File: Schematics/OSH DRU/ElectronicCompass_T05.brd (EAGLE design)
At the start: 50.5 x 50.8 mm, 69 parts, among them Q1 FDN360P, Q2 FDN360P, Q3 FDN360P, Q4 FDN360P, Q5 BC817-16LT1SMD, Q6 BC817-16LT1SMD, U1 ATMEGA32U4, U2 LTC4067, X1 USBSMD, Y1 16MHz

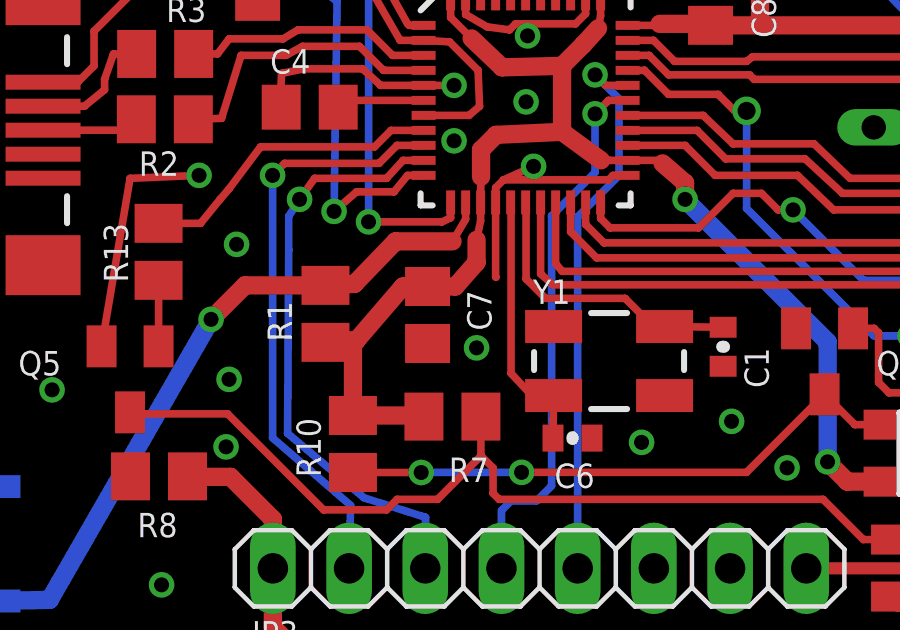
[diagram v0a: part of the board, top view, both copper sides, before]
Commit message: Removed capacitor
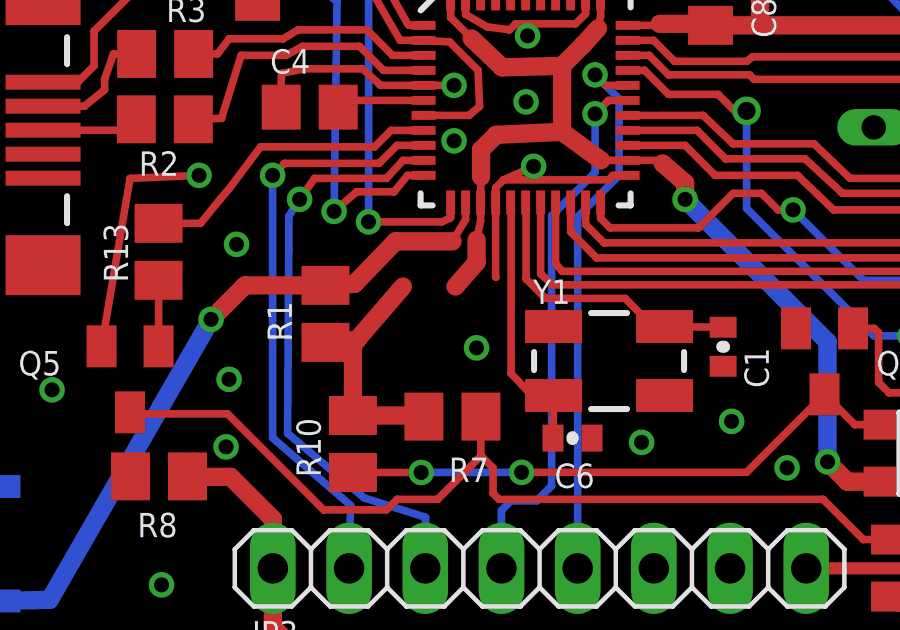
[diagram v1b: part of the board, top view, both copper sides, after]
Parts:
- removed C7: 0.1uF, rcl:C0805
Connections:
- net GND: no longer C7.2
- net VCC: no longer C7.1
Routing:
- net VCC: track 92.1 -> 90.3 mm
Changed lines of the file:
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@@
 <attribute name="NAME" x="27.2365" y="9.84275" size="0.8128" layer="25" rot="R180"/>
-</element>
-<element name="C7" library="rcl" package="C0805" value="0.1uF" x="21.66625" y="14.795" smashed="yes" rot="R270">
-<attribute name="NAME" x="22.98625" y="15.615" size="0.8128" layer="25" rot="R270"/>
 </element>
 <element name="R7" library="resistor" package="M0805" value="1M" x="22.495" y="11.4075" smashed="yes" rot="R180">
@@
 <contactref element="Q5" pad="E"/>
 <contactref element="Q6" pad="E"/>
-<contactref element="C7" pad="2"/>
 <contactref element="C8" pad="2"/>
 <contactref element="S2" pad="1"/>
@@
 <wire x1="27.7275" y1="36.8775" x2="27.95" y2="37.1" width="0.254" layer="1"/>
 <wire x1="27.95" y1="37.1" x2="28.973" y2="37.1" width="0.254" layer="1"/>
+<wire x1="44.45" y1="44.45" x2="47.6" y2="47.9" width="0" layer="19" extent="1-1"/>
+<wire x1="42.85" y1="47.25" x2="44.45" y2="44.45" width="0" layer="19" extent="1-1"/>
+<wire x1="45.005" y1="40.88625" x2="44.45" y2="44.45" width="0" layer="19" extent="1-1"/>
+<wire x1="45.05" y1="38.4" x2="45.005" y2="40.88625" width="0" layer="19" extent="1-1"/>
+<wire x1="41.15" y1="35.35" x2="45.05" y2="38.4" width="0" layer="19" extent="1-1"/>
+<wire x1="38.8" y1="35.75" x2="41.15" y2="35.35" width="0" layer="19" extent="1-1"/>
+<wire x1="36.5" y1="34.48" x2="38.8" y2="35.75" width="0" layer="19" extent="1-1"/>
+<wire x1="37.8" y1="38.65" x2="38.8" y2="35.75" width="0" layer="19" extent="1-1"/>
+<wire x1="34.205" y1="40.425" x2="37.8" y2="38.65" width="0" layer="19" extent="1-1"/>
+<wire x1="30.925" y1="40.255" x2="34.205" y2="40.425" width="0" layer="19" extent="1-1"/>
+<wire x1="30.2" y1="37.1" x2="30.925" y2="40.255" width="0" layer="19" extent="1-1"/>
+<wire x1="28.973" y1="36.6" x2="28.973" y2="37.1" width="0" layer="19" extent="1-1"/>
+<wire x1="28.973" y1="36.1" x2="28.973" y2="36.6" width="0" layer="19" extent="1-1"/>
+<wire x1="24.295" y1="40.225" x2="26.4975" y2="36.8775" width="0" layer="19" extent="1-1"/>
+<wire x1="31.055" y1="32.495" x2="28.973" y2="36.1" width="0" layer="19" extent="1-1"/>
+<wire x1="20.85" y1="37.25" x2="24.295" y2="40.225" width="0" layer="19" extent="1-1"/>
+<wire x1="45.85" y1="32.9" x2="41.15" y2="35.35" width="0" layer="19" extent="1-1"/>
+<wire x1="45.85" y1="30.35" x2="45.85" y2="32.9" width="0" layer="19" extent="1-1"/>
+<wire x1="31.1" y1="26.35" x2="31.055" y2="32.495" width="0" layer="19" extent="1-1"/>
+<wire x1="25" y1="24.1" x2="24.6" y2="24.5" width="0" layer="19" extent="1-1"/>
+<wire x1="28.85" y1="26.1" x2="27.7" y2="26.6" width="0" layer="19" extent="1-1"/>
+<wire x1="24.95" y1="21.9" x2="25" y2="24.1" width="0" layer="19" extent="1-1"/>
+<wire x1="25.2" y1="19.75" x2="24.95" y2="21.9" width="0" layer="19" extent="1-1"/>
+<wire x1="22.55" y1="20.6" x2="23.935" y2="19.035" width="0" layer="19" extent="1-1"/>
+<wire x1="22.55" y1="22.45" x2="22.55" y2="20.6" width="0" layer="19" extent="1-1"/>
+<wire x1="22.44875" y1="22.44875" x2="22.55" y2="22.45" width="0" layer="19" extent="1-1"/>
+<wire x1="16.78875" y1="21.7225" x2="16.75" y2="21.75" width="0" layer="19" extent="1-1"/>
+<wire x1="23.3" y1="13.7" x2="23.935" y2="16.065" width="0" layer="19" extent="1-1"/>
+<wire x1="16.0025" y1="25.25" x2="16.8" y2="22.85" width="0" layer="19" extent="1-1"/>
+<wire x1="14" y1="25.95" x2="16.0025" y2="25.25" width="0" layer="19" extent="1-1"/>
+<wire x1="19.6" y1="30.8" x2="22.2" y2="29.9" width="0" layer="19" extent="1-1"/>
+<wire x1="11.2" y1="27.3" x2="14" y2="25.95" width="0" layer="19" extent="1-1"/>
+<wire x1="34.25" y1="25.95" x2="31.1" y2="26.35" width="0" layer="19" extent="1-1"/>
+<wire x1="36.9" y1="27.8" x2="34.25" y2="25.95" width="0" layer="19" extent="1-1"/>
+<wire x1="39.37" y1="26.67" x2="36.9" y2="27.8" width="0" layer="19" extent="1-1"/>
+<wire x1="9.3" y1="30.2" x2="11.2" y2="27.3" width="0" layer="19" extent="1-1"/>
+<wire x1="14.05" y1="19.45" x2="16.75" y2="21.75" width="0" layer="19" extent="1-1"/>
+<wire x1="9.15" y1="12.3" x2="10.8" y2="13.75" width="0" layer="19" extent="1-1"/>
+<wire x1="15.3" y1="17.15" x2="14.05" y2="19.45" width="0" layer="19" extent="1-1"/>
+<wire x1="8.85" y1="19.355" x2="11.75" y2="19.35" width="0" layer="19" extent="1-1"/>
+<wire x1="7.335" y1="9.075" x2="9.15" y2="12.3" width="0" layer="19" extent="16-16"/>
+<wire x1="6.1" y1="14.55" x2="9.15" y2="12.3" width="0" layer="19" extent="1-1"/>
+<wire x1="11.765" y1="9.41625" x2="9.15" y2="12.3" width="0" layer="19" extent="1-1"/>
+<wire x1="14.95" y1="10.4" x2="11.765" y2="9.41625" width="0" layer="19" extent="1-1"/>
+<wire x1="15.05" y1="12.65" x2="14.95" y2="10.4" width="0" layer="19" extent="1-1"/>
+<wire x1="12.8" y1="5.8" x2="11.765" y2="9.41625" width="0" layer="19" extent="1-1"/>
+<wire x1="2.85" y1="12.2" x2="6.1" y2="14.55" width="0" layer="19" extent="1-1"/>
+<wire x1="6.1" y1="27.45" x2="9.3" y2="30.2" width="0" layer="19" extent="1-1"/>
+<wire x1="6.1" y1="33.65" x2="9.3" y2="30.2" width="0" layer="19" extent="1-1"/>
+<wire x1="2.1" y1="35.8" x2="6.1" y2="33.65" width="0" layer="19" extent="1-1"/>
+<wire x1="4.2" y1="38.4" x2="2.1" y2="35.8" width="0" layer="19" extent="1-1"/>
+<wire x1="10.65" y1="35.05" x2="6.1" y2="33.65" width="0" layer="19" extent="1-1"/>
+<wire x1="12.65" y1="38.5" x2="10.65" y2="35.05" width="0" layer="19" extent="1-1"/>
+<wire x1="12.3" y1="41.4" x2="12.65" y2="38.5" width="0" layer="19" extent="1-1"/>
+<wire x1="15.75" y1="41" x2="12.3" y2="41.4" width="0" layer="19" extent="1-1"/>
+<wire x1="27.1475" y1="10.69125" x2="23.3" y2="13.7" width="0" layer="19" extent="1-1"/>
+<wire x1="28.8" y1="10.55" x2="27.1475" y2="10.69125" width="0" layer="19" extent="1-1"/>
+<wire x1="31.8" y1="11.25" x2="28.8" y2="10.55" width="0" layer="19" extent="1-1"/>
+<wire x1="31.51875" y1="13.08625" x2="31.8" y2="11.25" width="0" layer="19" extent="1-1"/>
+<wire x1="33.65" y1="9.7" x2="31.8" y2="11.25" width="0" layer="19" extent="1-1"/>
+<wire x1="33.95" y1="14.35" x2="31.51875" y2="13.08625" width="0" layer="19" extent="1-1"/>
+<wire x1="31.75" y1="6.35" x2="33.65" y2="9.7" width="0" layer="19" extent="1-1"/>
+<wire x1="29.21" y1="6.35" x2="31.75" y2="6.35" width="0" layer="19" extent="1-1"/>
+<wire x1="30.25" y1="1.7" x2="29.21" y2="6.35" width="0" layer="19" extent="1-1"/>
+<wire x1="38.6" y1="13.05" x2="33.95" y2="14.35" width="0" layer="19" extent="1-1"/>
+<wire x1="39.5" y1="8.1" x2="38.6" y2="13.05" width="0" layer="19" extent="1-1"/>
+<wire x1="44" y1="7.1" x2="39.5" y2="8.1" width="0" layer="19" extent="1-1"/>
+<wire x1="47.5" y1="9.6" x2="44" y2="7.1" width="0" layer="19" extent="1-1"/>
+<wire x1="46.65" y1="13.4" x2="47.5" y2="9.6" width="0" layer="19" extent="1-1"/>
+<wire x1="9.2" y1="2.1" x2="12.8" y2="5.8" width="0" layer="19" extent="1-1"/>
+<wire x1="12" y1="46.6" x2="12.3" y2="41.4" width="0" layer="19" extent="1-1"/>
+<wire x1="43.95" y1="1.9" x2="44" y2="7.1" width="0" layer="19" extent="1-1"/>
+<wire x1="36.54" y1="21.05" x2="34.25" y2="25.95" width="0" layer="19" extent="1-1"/>
+<wire x1="16.7" y1="1.9" x2="12.8" y2="5.8" width="0" layer="19" extent="1-1"/>
+<wire x1="23.9" y1="1.9" x2="30.25" y2="1.7" width="0" layer="19" extent="1-1"/>
+<wire x1="2.7" y1="2.2" x2="9.2" y2="2.1" width="0" layer="19" extent="1-1"/>
+<wire x1="5.45" y1="47.05" x2="12" y2="46.6" width="0" layer="19" extent="1-1"/>
+<wire x1="2" y1="48.65" x2="5.45" y2="47.05" width="0" layer="19" extent="1-1"/>
+<wire x1="37.35" y1="1.9" x2="39.5" y2="8.1" width="0" layer="19" extent="1-1"/>
 </signal>
 <signal name="VCC">
@@
 <contactref element="U1" pad="24"/>
 <contactref element="U1" pad="44"/>
-<contactref element="C7" pad="1"/>
 <contactref element="R11" pad="2"/>
 <contactref element="S3" pad="2"/>
@@
 <wire x1="18.33625" y1="13.955" x2="19.3" y2="13.95" width="0.6096" layer="1"/>
 <wire x1="19.3" y1="13.95" x2="20.845" y2="15.745" width="0.6096" layer="1"/>
-<wire x1="20.845" y1="15.745" x2="21.66625" y2="15.745" width="0.6096" layer="1"/>
 <wire x1="19.18" y1="11.445" x2="21.5075" y2="11.445" width="0.6096" layer="1"/>
 <wire x1="21.5075" y1="11.445" x2="21.545" y2="11.4075" width="0.6096" layer="1"/>
@@
 <wire x1="29.39875" y1="19.94875" x2="29.5" y2="19.85" width="0.254" layer="1"/>
 <wire x1="23.3" y1="16.55" x2="22.595" y2="15.745" width="0.6096" layer="1"/>
-<wire x1="22.595" y1="15.745" x2="21.66625" y2="15.745" width="0.6096" layer="1"/>
 <wire x1="19.3" y1="13.95" x2="19.18" y2="13.83" width="0.6096" layer="1"/>
 <wire x1="19.18" y1="13.83" x2="19.18" y2="11.445" width="0.6096" layer="1"/>
+<wire x1="20.845" y1="15.745" x2="22.595" y2="15.745" width="0" layer="19" extent="1-1"/>
 </signal>
 <signal name="UCAP">
